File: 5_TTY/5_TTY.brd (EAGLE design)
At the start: 67.4 x 44.8 mm, 27 parts, among them Q2 BC857C, Q3 BC857C, Q4 BC857C, Q5 BC857C, Q6 BC857C, T4 BC847, X11 ALLSERIALD, X7 AKL18X-04W

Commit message: new BOMs,
finish TTY board
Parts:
- removed SV5: (no value), con-ml:ML14L
- added R1, R2: 33R, resistor:R0805
- added SV1: (no value), con-lstb:MA08-2W
- R18: value 10k -> 180k
- R20: value 1k -> 4k7
- moved Q4 57.6 mm to (1.27, 26.7), turned to 180 degrees
- moved R15 45.8 mm to (-3.81, 21.6), turned to 90 degrees
- moved R16 44.9 mm to (1.27, 17.8), turned to 180 degrees
- moved R14 37.5 mm to (-7.62, 17.8), turned to 180 degrees
- moved T4 37.1 mm to (-19.1, 22.9)
- moved Q3 36.1 mm to (-7.62, 21.6)
- moved Q2 35.4 mm to (-7.62, 26.7), turned to 180 degrees
- moved R10 33.8 mm to (-21.0, 19.1)
- moved Q5 30.6 mm to (-21.6, 2.54), turned to 90 degrees
- moved R11 27.0 mm to (-25.4, 19.1), turned to 180 degrees
- moved R13 25.0 mm to (-16.5, 3.81), turned to 180 degrees
- moved D1 21.6 mm to (-22.9, 22.9), turned to 180 degrees
- moved R12 14.8 mm to (-27.3, 22.9), turned to 90 degrees
- moved R19 13.7 mm to (19.1, 27.9)
- moved Q6 10.8 mm to (1.27, 21.6)
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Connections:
- new net CS1: R1.1, SV1.3
- new net CS2: R2.1, SV1.4
- net +12V: now also SV1.1, SV1.2
- net CC1: now also SV1.15; no longer SV5.13
- net CC2: now also SV1.16; no longer SV5.14
- net GND: now also R18.2, SV1.10, SV1.9; no longer SV5.7, SV5.8
- net N$44: now also SV1.11, X7.P$2; no longer SV5.9
- net N$46: no longer R18.2
- net N$49: now also R2.2
- net N$59: now also R1.2
- net N$65: now also SV1.12, X7.P$4; no longer SV5.10
- net RXN: now also SV1.7, X7.P$3; no longer SV5.5
- net RXP: now also SV1.14, SV1.6; no longer SV5.12, SV5.4
- net TXN: now also SV1.8, X7.P$1; no longer SV5.6
- net TXP: now also SV1.13, SV1.5; no longer SV5.11, SV5.3
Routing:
- net TXN: track 0.00 -> 84.5 mm, vias 0 -> 1
- net RXN: track 0.00 -> 69.0 mm
- net +12V: track 0.00 -> 63.9 mm, vias 0 -> 3
- net N$56: track 0.00 -> 54.6 mm, vias 0 -> 2
- net N$58: track 0.00 -> 50.1 mm
- net TXP: track 0.00 -> 47.9 mm
- net +5V: track 0.00 -> 45.0 mm
- net CS2: track 0.00 -> 43.9 mm
- net RXP: track 0.00 -> 41.4 mm
- net N$44: track 0.00 -> 38.5 mm
- net N$91: track 0.00 -> 33.1 mm
- net N$65: track 0.00 -> 27.2 mm
- net CS1: track 0.00 -> 26.3 mm
- net N$63: track 0.00 -> 24.4 mm, vias 0 -> 1
- net N$64: track 0.00 -> 21.9 mm
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- added copper zone on layer 16, net GND

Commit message: add author
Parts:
- renumbered SV1 to X2, X11 to X1
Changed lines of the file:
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@@
 <?xml version="1.0" encoding="utf-8"?>
 <!DOCTYPE eagle SYSTEM "eagle.dtd">
-<eagle version="7.6.0">
+<eagle version="7.7.0">
 <drawing>
 <settings>
@@
 </element>
 <element name="U$7" library="Mentor" package="1296.2012" value="" x="5.08" y="39.37" smashed="yes"/>
-<element name="X11" library="AllSerial" package="DAUGHTER-THT" value="ALLSERIALD" x="0" y="0" smashed="yes">
+<element name="X1" library="AllSerial" package="DAUGHTER-THT" value="ALLSERIALD" x="0" y="0" smashed="yes">
 <attribute name="NAME" x="13.0175" y="1.5875" size="1.016" layer="25" ratio="10"/>
 </element>
-<element name="SV1" library="con-lstb" package="MA08-2W" value="" x="-13.97" y="34.925" smashed="yes">
+<element name="X2" library="con-lstb" package="MA08-2W" value="" x="-13.97" y="34.925" smashed="yes">
 <attribute name="MF" value="" x="-13.97" y="34.925" size="1.778" layer="27" display="off"/>
 <attribute name="OC_FARNELL" value="unknown" x="-13.97" y="34.925" size="1.778" layer="27" display="off"/>
@@
 <contactref element="R11" pad="2"/>
 <contactref element="T4" pad="2"/>
-<contactref element="SV1" pad="8"/>
+<contactref element="X2" pad="8"/>
 <contactref element="X7" pad="P$1"/>
 <wire x1="-19.05" y1="15.24" x2="-19.05" y2="14.605" width="0.3048" layer="1"/>
@@
 <contactref element="D1" pad="3"/>
 <contactref element="R10" pad="1"/>
-<contactref element="SV1" pad="5"/>
-<contactref element="SV1" pad="13"/>
+<contactref element="X2" pad="5"/>
+<contactref element="X2" pad="13"/>
 <wire x1="-17.78" y1="33.655" x2="-16.51" y2="34.925" width="0.3048" layer="1"/>
 <wire x1="-16.51" y1="34.925" x2="-8.89" y2="34.925" width="0.3048" layer="1"/>
@@
 <signal name="CC1">
 <contactref element="Q2" pad="C"/>
-<contactref element="SV1" pad="15"/>
+<contactref element="X2" pad="15"/>
 <wire x1="-5.08" y1="33.655" x2="-5.08" y2="31.75" width="0.3048" layer="1"/>
 <wire x1="-5.08" y1="31.75" x2="-7.62" y2="29.21" width="0.3048" layer="1"/>
@@
 <signal name="CC2">
 <contactref element="Q4" pad="C"/>
-<contactref element="SV1" pad="16"/>
+<contactref element="X2" pad="16"/>
 <wire x1="-5.08" y1="36.195" x2="-1.905" y2="36.195" width="0.3048" layer="1"/>
 <wire x1="-1.905" y1="36.195" x2="1.27" y2="33.02" width="0.3048" layer="1"/>
@@
 <contactref element="R19" pad="1"/>
 <contactref element="D2" pad="3"/>
-<contactref element="SV1" pad="6"/>
-<contactref element="SV1" pad="14"/>
+<contactref element="X2" pad="6"/>
+<contactref element="X2" pad="14"/>
 <wire x1="-17.78" y1="36.195" x2="-16.51" y2="37.465" width="0.3048" layer="1"/>
 <wire x1="-16.51" y1="37.465" x2="-8.89" y2="37.465" width="0.3048" layer="1"/>
@@
 <contactref element="OK1" pad="2"/>
 <contactref element="D2" pad="1"/>
-<contactref element="SV1" pad="7"/>
+<contactref element="X2" pad="7"/>
 <contactref element="X7" pad="P$3"/>
 <wire x1="-15.24" y1="33.655" x2="-13.97" y2="34.925" width="0.3048" layer="16"/>
@@
 <contactref element="OK1" pad="4"/>
 <contactref element="R20" pad="2"/>
-<contactref element="X11" pad="8"/>
+<contactref element="X1" pad="8"/>
 <wire x1="13.015" y1="10.16" x2="13.015" y2="11.115" width="0.3048" layer="1"/>
 <wire x1="13.015" y1="11.115" x2="12.7" y2="11.43" width="0.3048" layer="1"/>
@@
 </signal>
 <signal name="N$91">
-<contactref element="X11" pad="5"/>
+<contactref element="X1" pad="5"/>
 <contactref element="Q5" pad="B"/>
 <wire x1="-20.49" y1="1.59" x2="6.035" y2="1.59" width="0.3048" layer="1"/>
@@
 </signal>
 <signal name="GND">
-<contactref element="X11" pad="19"/>
+<contactref element="X1" pad="19"/>
 <contactref element="R15" pad="1"/>
 <contactref element="R17" pad="1"/>
 <contactref element="OK3" pad="2"/>
 <contactref element="R20" pad="1"/>
-<contactref element="SV1" pad="10"/>
-<contactref element="SV1" pad="9"/>
+<contactref element="X2" pad="10"/>
+<contactref element="X2" pad="9"/>
 <polygon width="0.254" layer="16">
 <vertex x="-34.29" y="0"/>
@@
 </signal>
 <signal name="+5V">
-<contactref element="X11" pad="7"/>
-<contactref element="X11" pad="18"/>
+<contactref element="X1" pad="7"/>
+<contactref element="X1" pad="18"/>
 <contactref element="R13" pad="1"/>
 <contactref element="OK1" pad="5"/>
@@
 </signal>
 <signal name="+12V">
-<contactref element="X11" pad="20"/>
+<contactref element="X1" pad="20"/>
 <contactref element="Q3" pad="E"/>
 <contactref element="R14" pad="1"/>
 <contactref element="Q6" pad="E"/>
 <contactref element="R16" pad="1"/>
-<contactref element="SV1" pad="1"/>
-<contactref element="SV1" pad="2"/>
+<contactref element="X2" pad="1"/>
+<contactref element="X2" pad="2"/>
 <wire x1="-22.86" y1="36.195" x2="-22.86" y2="33.655" width="0.3048" layer="1"/>
 <wire x1="-6.67" y1="20.49" x2="-6.67" y2="17.78" width="0.3048" layer="1"/>
@@
 <signal name="CS1">
 <contactref element="R1" pad="1"/>
-<contactref element="SV1" pad="3"/>
+<contactref element="X2" pad="3"/>
 <wire x1="-20.32" y1="33.655" x2="-20.32" y2="31.75" width="0.3048" layer="1"/>
 <wire x1="-20.32" y1="31.75" x2="-12.065" y2="23.495" width="0.3048" layer="1"/>
@@
 <signal name="CS2">
 <contactref element="R2" pad="1"/>
-<contactref element="SV1" pad="4"/>
+<contactref element="X2" pad="4"/>
 <wire x1="-20.32" y1="36.195" x2="-21.59" y2="34.925" width="0.3048" layer="1"/>
 <wire x1="-21.59" y1="34.925" x2="-21.59" y2="31.75" width="0.3048" layer="1"/>
@@
 </signal>
 <signal name="N$44">
-<contactref element="SV1" pad="11"/>
+<contactref element="X2" pad="11"/>
 <contactref element="X7" pad="P$2"/>
 <wire x1="-10.16" y1="33.655" x2="-8.89" y2="34.925" width="0.3048" layer="16"/>
@@
 </signal>
 <signal name="N$65">
-<contactref element="SV1" pad="12"/>
+<contactref element="X2" pad="12"/>
 <contactref element="X7" pad="P$4"/>
 <wire x1="-10.16" y1="36.195" x2="-10.16" y2="38.1" width="0.3048" layer="16"/>

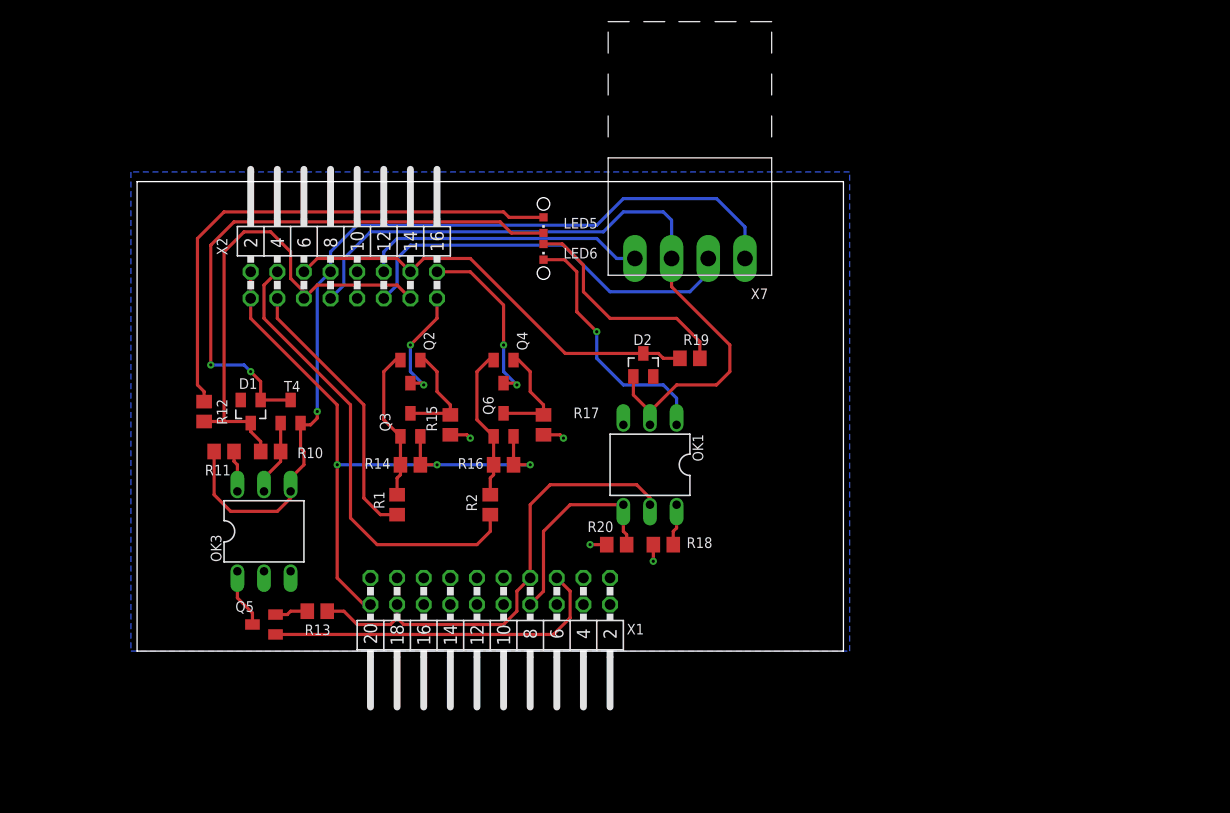
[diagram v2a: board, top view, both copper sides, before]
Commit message: change to libv2
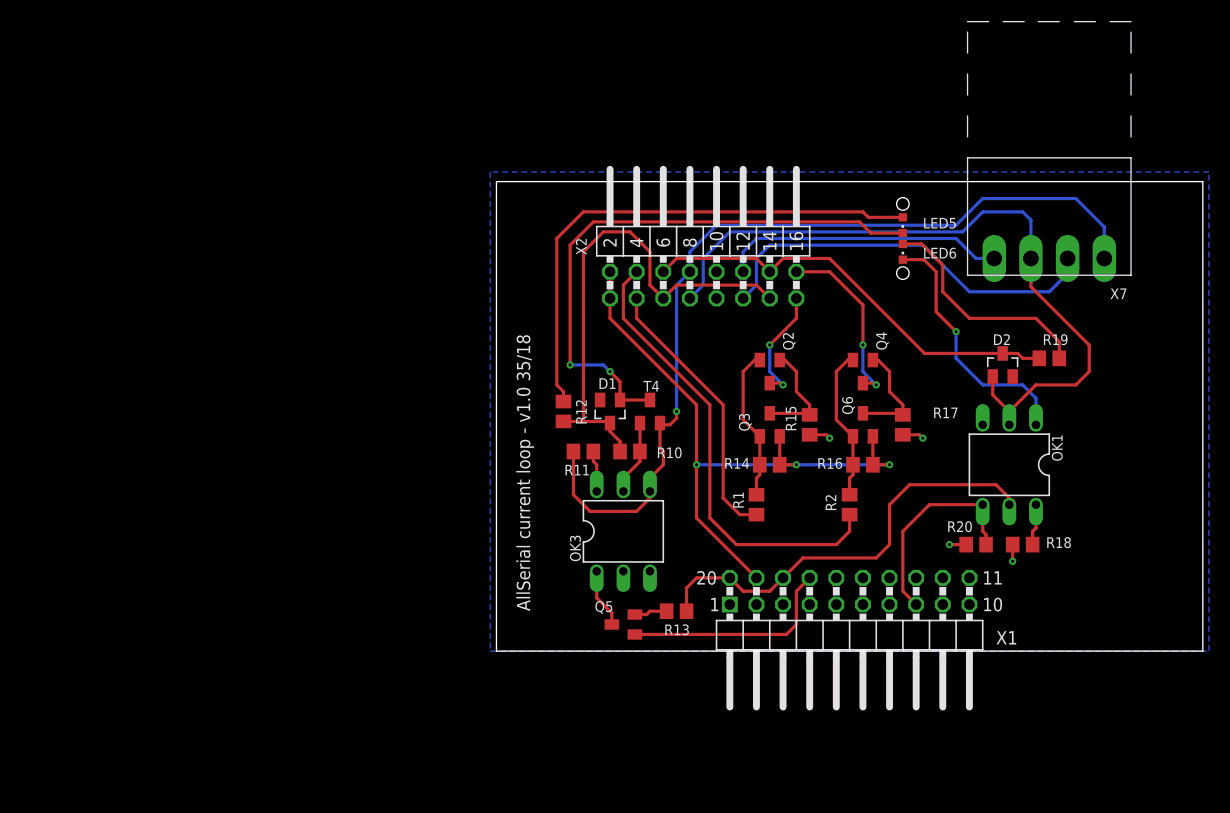
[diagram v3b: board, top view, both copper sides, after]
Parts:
- X1: value ALLSERIALD -> ALLSERIALSLAVE; device AllSerial:DAUGHTER-THT -> AllSerialv2:DAUGHTER-THT
- moved D2 34.3 mm to (48.9, 27.3)
- moved R13 34.3 mm to (17.8, 3.81)
- moved R19 34.3 mm to (53.3, 27.9)
- moved X7 34.3 mm to (53.3, 37.5)
- moved D1 34.3 mm to (11.4, 22.9)
- moved LED5 34.3 mm to (39.4, 40.6)
- moved LED6 34.3 mm to (39.4, 38.1)
- moved OK1 34.3 mm to (49.5, 17.8)
- moved OK3 34.3 mm to (12.7, 11.4)
- moved Q2 34.3 mm to (26.7, 26.7)
- moved Q3 34.3 mm to (26.7, 21.6)
- moved Q4 34.3 mm to (35.6, 26.7)
- moved Q5 34.3 mm to (12.7, 2.54)
- moved Q6 34.3 mm to (35.6, 21.6)
- moved R1 34.3 mm to (25.4, 14.0)
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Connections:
- net +12V: now also X1.19; no longer X1.20
- net +5V: now also X1.20; no longer X1.7
- net GND: now also X1.1; no longer X1.19
- net N$91: now also X1.17; no longer X1.5
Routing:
- net N$91: track 33.1 -> 20.8 mm
- net +5V: track 45.0 -> 41.5 mm
- net +12V: track 63.9 -> 62.0 mm
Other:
- board text added: "AllSerial current loop - v1.0 35/18"

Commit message: final design & order
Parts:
- removed OK3: 4N25, optocoupler:DIL06
- removed X7: AKL18X-04W, con-riacon_akl:AKL182-04
- added OK2: 4N25, optocoupler:DIL06
- added R3, R4: 68R, resistor:R0805
- added X3: MA03-2W, con-lstb:MA03-2W
- R1, R2: value 33R -> 15R
- R14: value 33R -> 68R
- X2: value (none) -> AKL18X-08W; device con-lstb:MA08-2W -> con-riacon_akl:AKL182-08
- moved D1 28.7 mm to (39.4, 29.2)
- moved R10 28.7 mm to (41.3, 25.4)
- moved R11 28.7 mm to (36.8, 25.4)
- moved T4 28.7 mm to (43.2, 29.2)
- moved R12 28.5 mm to (34.9, 28.6), turned to 180 degrees
- moved R19 28.4 mm to (27.9, 40.6), turned to 90 degrees
- moved R16 26.9 mm to (8.89, 21.6), turned to 90 degrees
- moved R17 26.9 mm to (12.7, 17.8), turned to 0 degrees
- moved R2 26.4 mm to (12.7, 29.2), turned to 270 degrees
- moved X2 25.5 mm to (45.7, 37.5), turned to 180 degrees
- moved R1 23.4 mm to (7.62, 29.2), turned to 270 degrees
- moved Q6 22.9 mm to (12.7, 21.6), turned to 270 degrees
- moved R15 21.8 mm to (12.7, 8.89), turned to 0 degrees
- moved Q5 21.0 mm to (31.8, 11.4), turned to 0 degrees
- moved R13 20.1 mm to (36.8, 10.2)
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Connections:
- removed net CS1: R1.1, X2.3
- removed net CS2: R2.1, X2.4
- removed net N$44: X2.11, X7.P$2
- removed net N$65: X2.12, X7.P$4
- removed net RXN: D2.1, OK1.2, X2.7, X7.P$3
- removed net RXP: D2.3, R19.1, X2.14, X2.6
- removed net TXN: OK3.4, R11.2, T4.2, X2.8, X7.P$1
- new net N$2: R1.1, X3.2
- new net N$3: R2.1, X3.1
- new net N$4: OK2.4, R11.2, T4.2, X2.P$6
- new net N$5: R3.1, X3.6
- new net N$6: R4.1, X3.5
- new net N$7: D2.3, R19.1, X2.P$3
- new net N$8: D2.1, OK1.2, X2.P$2
- net +12V: now also X3.3, X3.4; no longer X2.1, X2.2
- net CC1: now also X2.P$4; no longer X2.15
- net CC2: now also X2.P$8; no longer X2.16
- net GND: now also OK2.2, X2.P$1, X2.P$5; no longer OK3.2, X2.10, X2.9
- net N$49: now also R4.2
- net N$54: now also OK2.6; no longer OK3.6
- net N$55: now also OK2.5; no longer OK3.5
- net N$59: now also R3.2
- net N$60: now also OK2.1; no longer OK3.1
- net TXP: now also X2.P$7; no longer X2.13, X2.5
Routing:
- net TXN: track 84.5 -> 0.00 mm, vias 1 -> 0
- net RXN: track 69.0 -> 0.00 mm
- net CS2: track 43.9 -> 0.00 mm
- net RXP: track 41.4 -> 0.00 mm
- net CC1: track 11.2 -> 51.3 mm, vias 2 -> 4
- net N$44: track 38.5 -> 0.00 mm
- net N$58: track 50.1 -> 15.0 mm
- net N$7: track 0.00 -> 35.0 mm, vias 0 -> 1
- net N$4: track 0.00 -> 33.7 mm, vias 0 -> 1
- net TXP: track 47.9 -> 16.1 mm, vias 0 -> 1
- net N$56: track 54.6 -> 24.1 mm
- net N$65: track 27.2 -> 0.00 mm
- net CS1: track 26.3 -> 0.00 mm
- net N$63: track 24.4 -> 46.6 mm, vias 1 -> 0
- net N$8: track 0.00 -> 18.7 mm, vias 0 -> 1
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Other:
- board text added: "AllSerial current loop - v1.1 39/18"
- board text removed: "AllSerial current loop - v1.0 35/18"
